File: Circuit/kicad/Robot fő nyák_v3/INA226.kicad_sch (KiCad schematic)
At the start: 32 parts, among them U10 INA226, U11 INA226, U13 INA226, U14 INA226, U15 INA226, U16 INA226, U34 INA226, U35 INA226, U36 INA226, U37 INA226, U38 INA226, U39 INA226, U4 INA226, U40 INA226, U41 INA226, U9 INA226

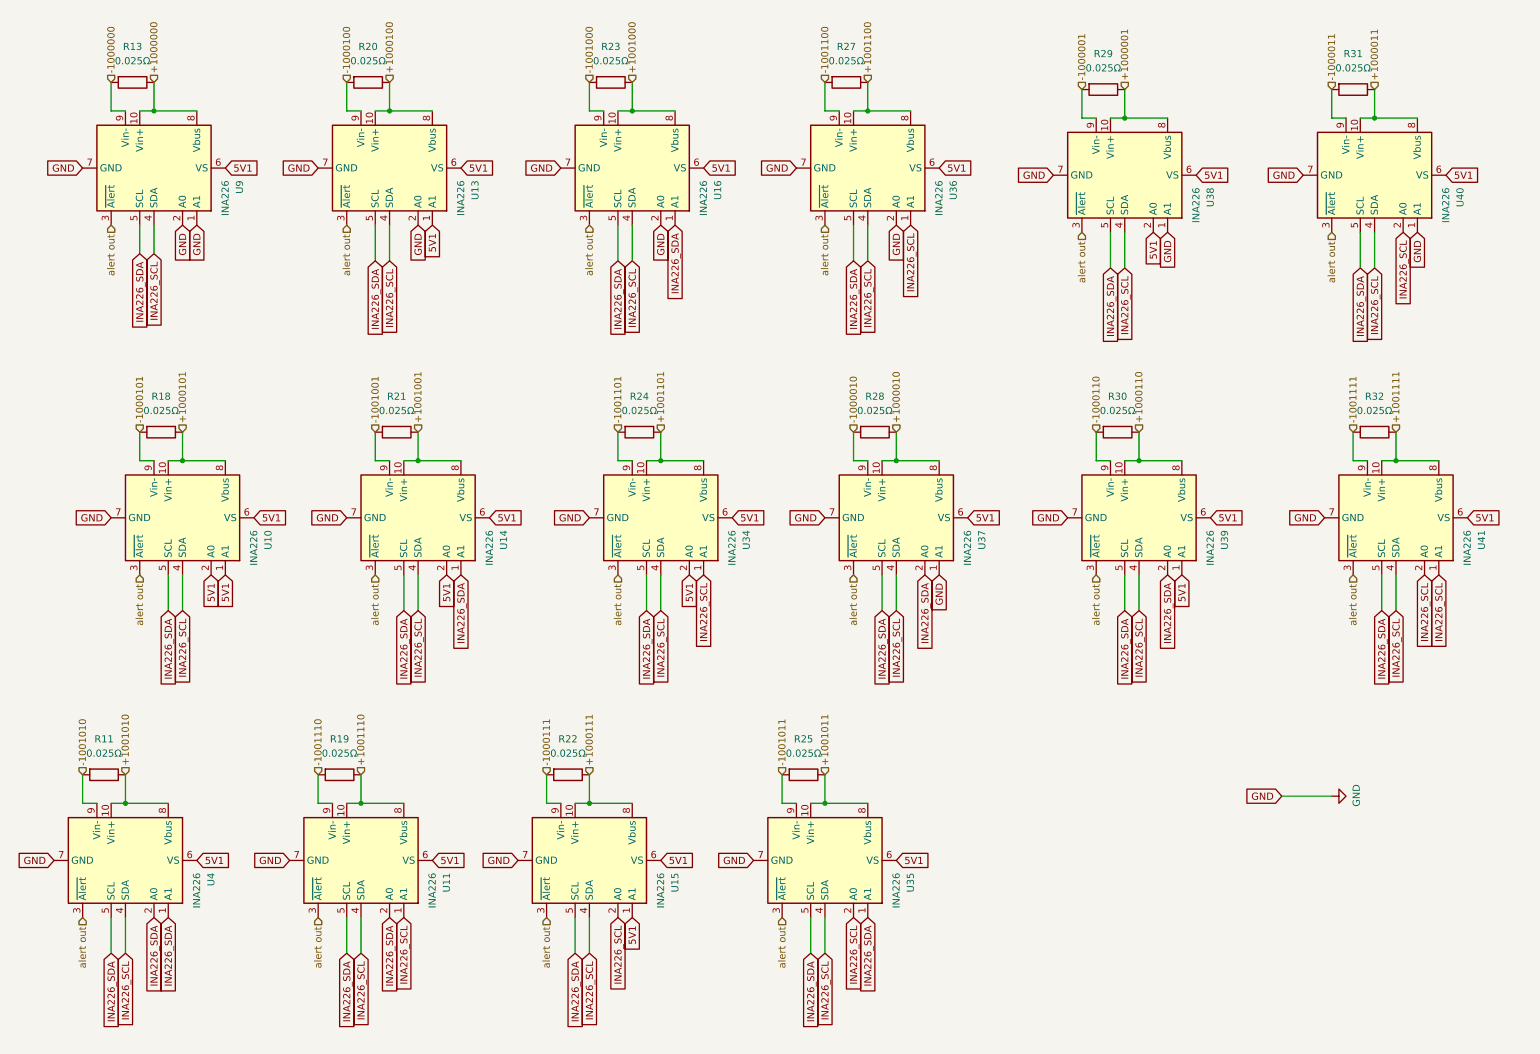
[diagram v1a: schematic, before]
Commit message: KICAD V3.01 Cleaned sheets + update + szekér modell add
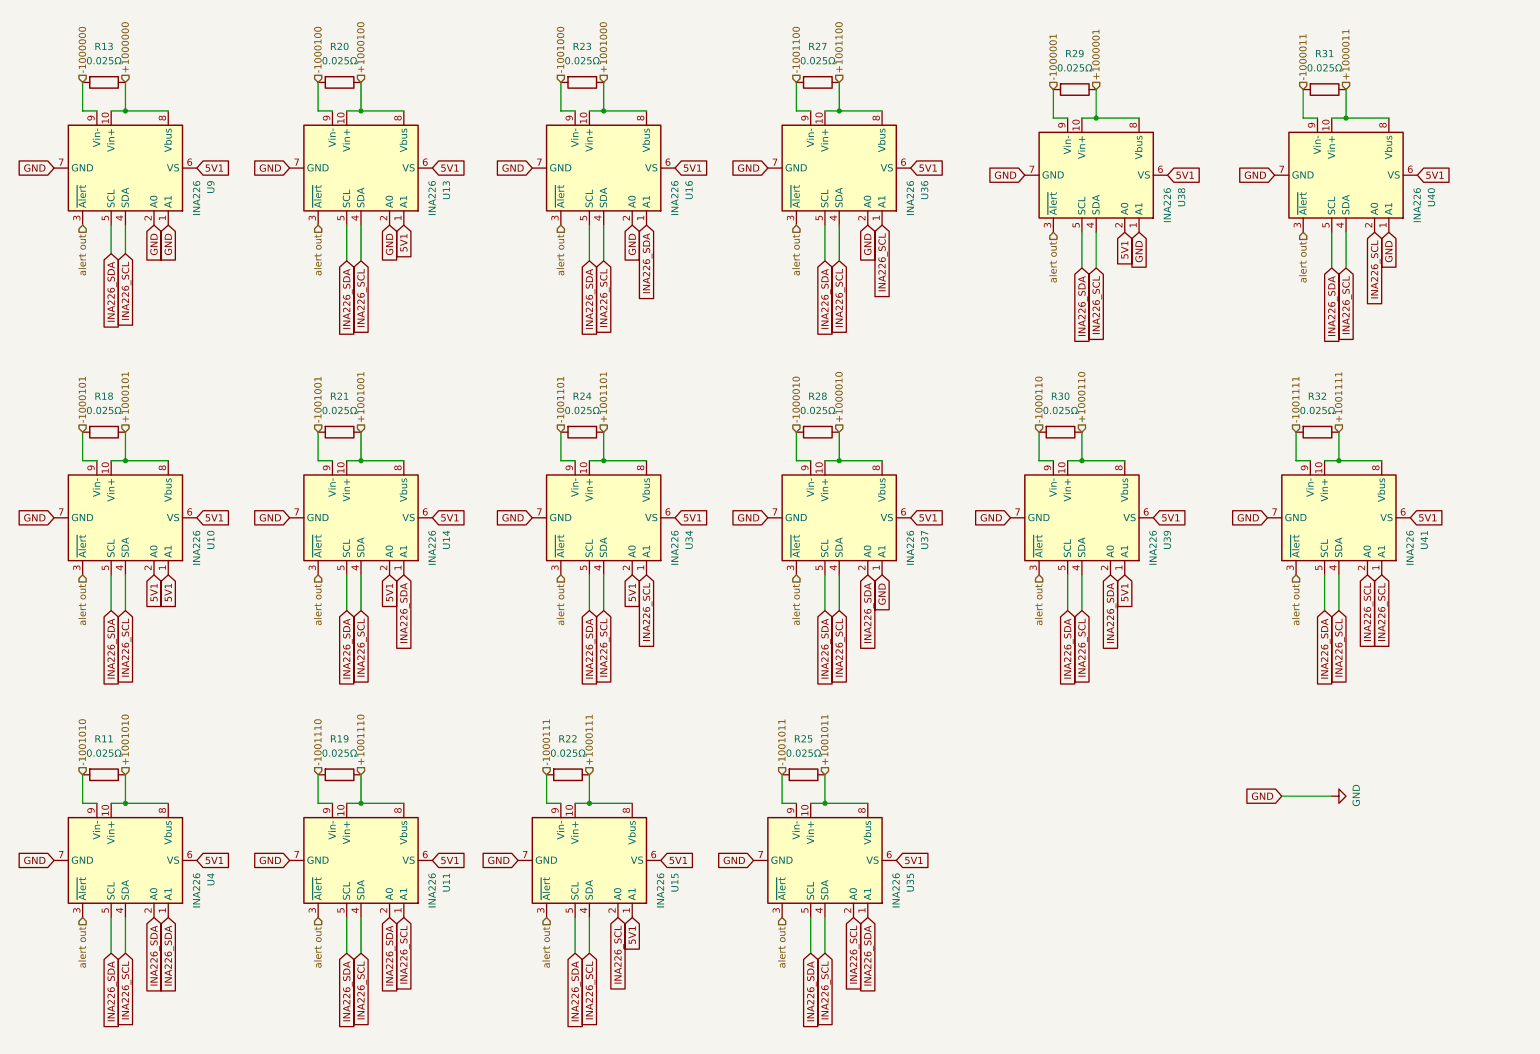
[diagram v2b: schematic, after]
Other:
- moved on the sheet: R13, R18, R20, R21, R23, R24, R27, R28, R29, R30, R31, R32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

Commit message: kicad v0.1 footprint- assing spi finish
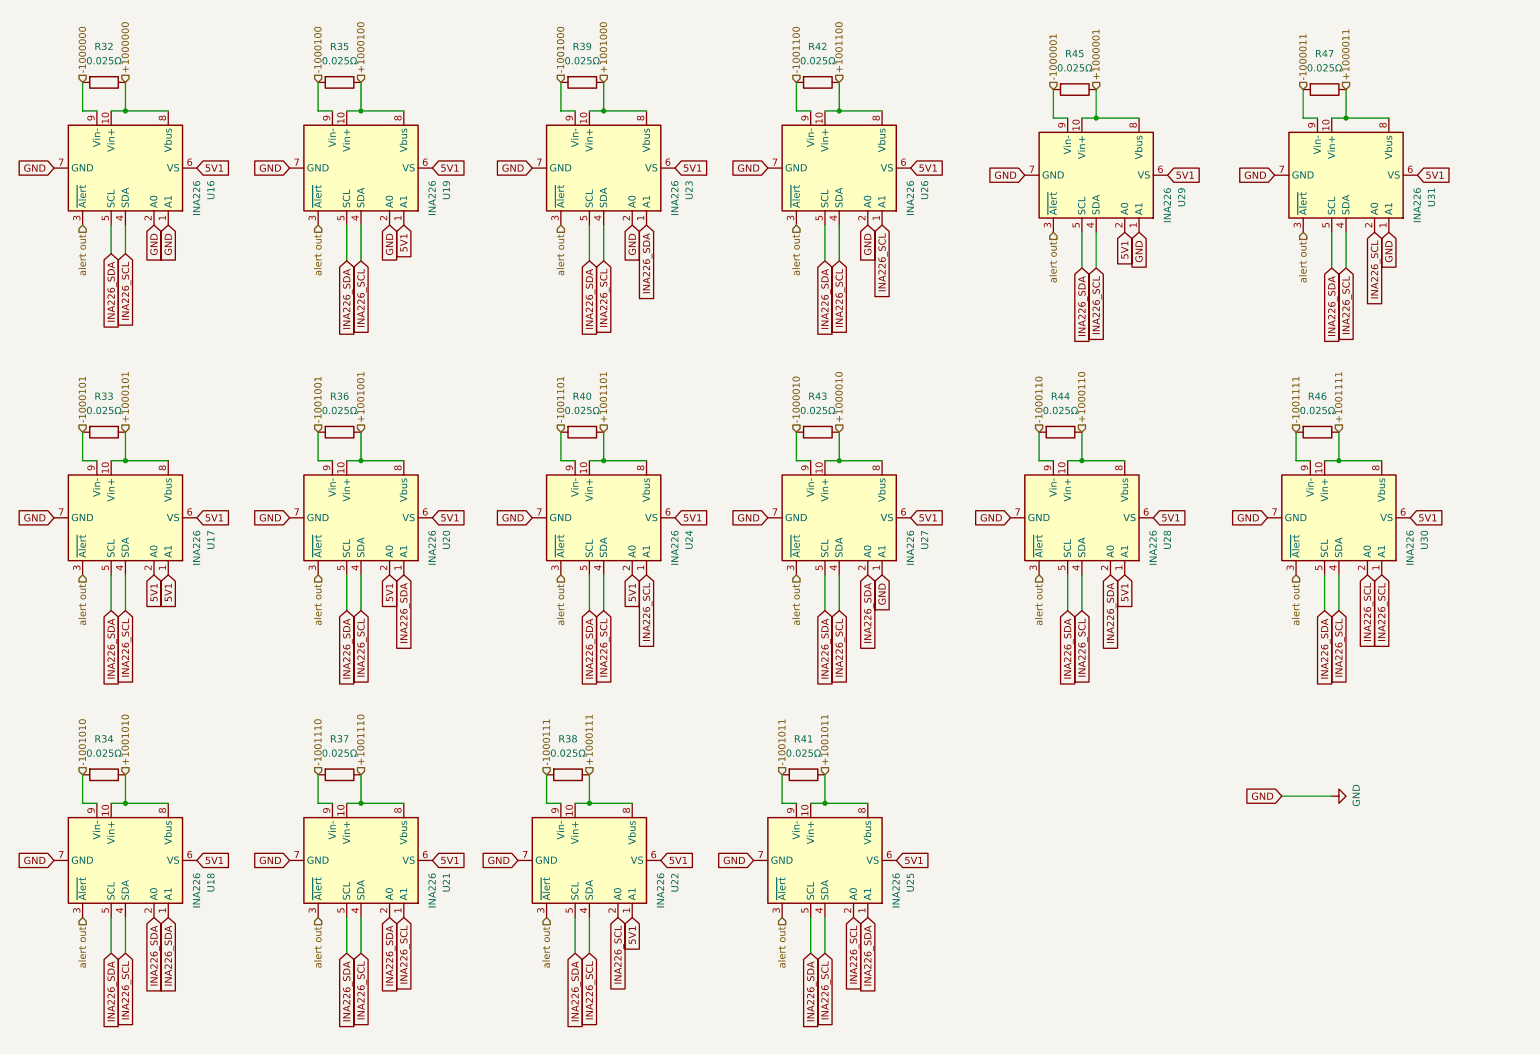
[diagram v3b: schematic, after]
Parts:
- R32: renamed from R13; footprint Resistor_SMD:R_1020_2550Metric -> Resistor_SMD:R_1206_3216Metric
- R33: renamed from R18; footprint Resistor_SMD:R_1020_2550Metric -> Resistor_SMD:R_1206_3216Metric
- R34: renamed from R11; footprint Resistor_SMD:R_1020_2550Metric -> Resistor_SMD:R_1206_3216Metric
- R36: renamed from R21; footprint Resistor_SMD:R_1020_2550Metric -> Resistor_SMD:R_1206_3216Metric
- R37: renamed from R19; footprint Resistor_SMD:R_1020_2550Metric -> Resistor_SMD:R_1206_3216Metric
- R38: renamed from R22; footprint Resistor_SMD:R_1020_2550Metric -> Resistor_SMD:R_1206_3216Metric
- R39: renamed from R23; footprint Resistor_SMD:R_1020_2550Metric -> Resistor_SMD:R_1206_3216Metric
- R40: renamed from R24; footprint Resistor_SMD:R_1020_2550Metric -> Resistor_SMD:R_1206_3216Metric
- R41: renamed from R25; footprint Resistor_SMD:R_1020_2550Metric -> Resistor_SMD:R_1206_3216Metric
- R42: renamed from R27; footprint Resistor_SMD:R_1020_2550Metric -> Resistor_SMD:R_1206_3216Metric
- R43: renamed from R28; footprint Resistor_SMD:R_1020_2550Metric -> Resistor_SMD:R_1206_3216Metric
- R44: renamed from R30; footprint Resistor_SMD:R_1020_2550Metric -> Resistor_SMD:R_1206_3216Metric
- R45: renamed from R29; footprint Resistor_SMD:R_1020_2550Metric -> Resistor_SMD:R_1206_3216Metric
- R46: renamed from R32; footprint Resistor_SMD:R_1020_2550Metric -> Resistor_SMD:R_1206_3216Metric
- R47: renamed from R31; footprint Resistor_SMD:R_1020_2550Metric -> Resistor_SMD:R_1206_3216Metric
- renumbered R20 to R35, U9 to U16, U10 to U17, U4 to U18, U13 to U19, U14 to U20, U11 to U21, U15 to U22, U16 to U23, U34 to U24, U35 to U25, U36 to U26, U37 to U27, U39 to U28, U38 to U29, U41 to U30, U40 to U31

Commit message: kicad update new readme media updates the circuit is 95% finished
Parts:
- added C100, C101, C102, C103, C104, C105, C106, C107, C92, C93, C94, C95, C96, C97, C98, C99: 1uf, Capacitor_SMD:C_0805_2012Metric, symbol Device:C
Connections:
- net 5V1: now also C100.2, C101.2, C102.2, C103.2, C104.2, C105.2, C106.2, C107.2, C92.1, C93.1, C94.1, C95.1, C96.1, C97.1, C98.1, C99.1
- net GND: now also C100.1, C101.1, C102.1, C103.1, C104.1, C105.1, C106.1, C107.1, C92.2, C93.2, C94.2, C95.2, C96.2, C97.2, C98.2, C99.2

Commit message: readme updated kicad circuit V1
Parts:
- R36: renamed from R35; footprint Resistor_SMD:R_1020_2550Metric -> Resistor_SMD:R_1206_3216Metric
- renumbered C92 to C22, C100 to C23, C93 to C24, C101 to C25, C94 to C26, C102 to C27, C95 to C28, C103 to C29, C96 to C30, C104 to C31, C97 to C32, C105 to C33, C98 to C34, C106 to C35, C99 to C36, C107 to C37, R32 to R33, R33 to R34, R34 to R35, R36 to R37, R37 to R38, R38 to R39, R39 to R40, R40 to R41, R41 to R42, R42 to R43, R43 to R44, R44 to R45, R45 to R46, R46 to R47, R47 to R48, U16 to U15, U17 to U16, U18 to U17, U19 to U18, U20 to U19, U21 to U20, U22 to U21, U23 to U22, U24 to U23, U25 to U24, U26 to U25, U27 to U26, U28 to U27, U29 to U28, U30 to U29, U31 to U30
